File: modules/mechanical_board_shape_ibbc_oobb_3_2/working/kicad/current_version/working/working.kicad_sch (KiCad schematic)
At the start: 4 parts

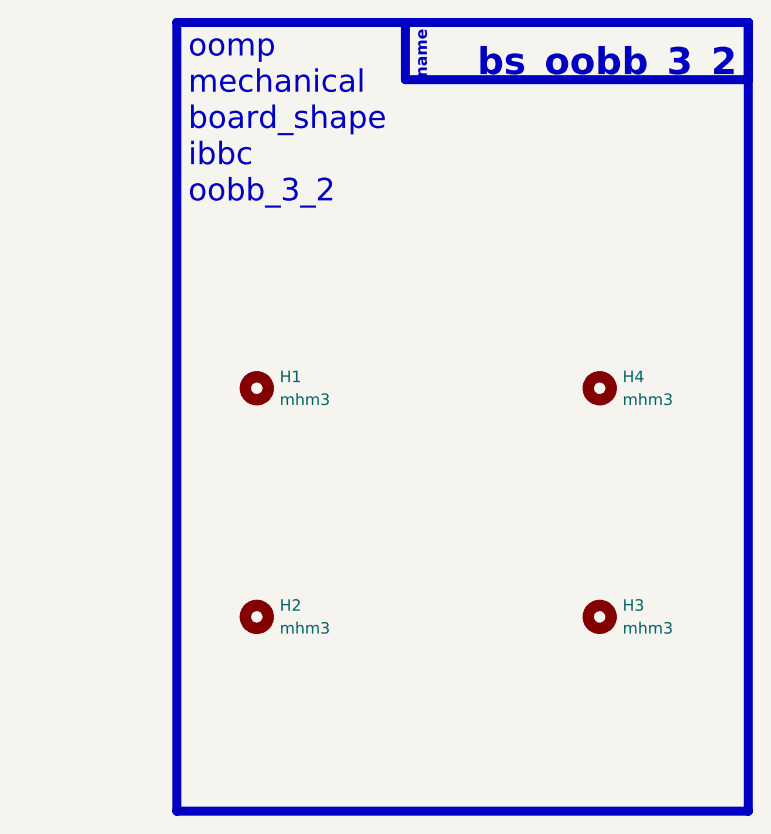
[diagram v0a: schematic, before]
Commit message: fixed formatting to be more consistent
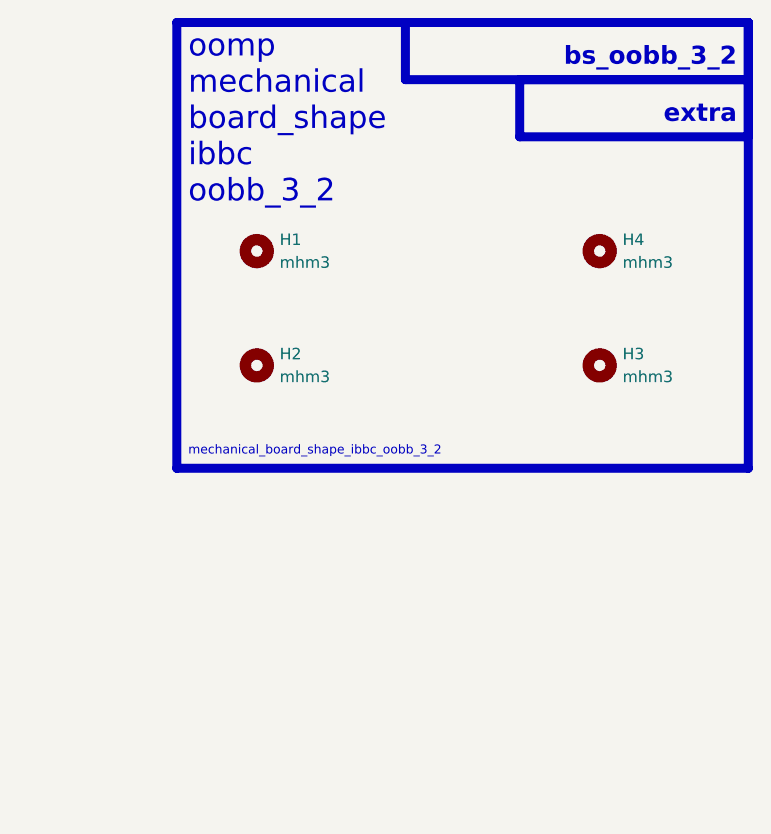
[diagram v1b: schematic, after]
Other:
- note added: "extra"
- note added: "mechanical_board_shape_ibbc_oobb_3_2"
- note removed: "name"
- moved on the sheet: H1, H2, H3, H4
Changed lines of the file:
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@@
 (kicad_sch (version 20230121) (generator eeschema)
   (paper "A4")
-  (rectangle (start 93.98 17.78) (end 157.48 105.41)
+  (rectangle (start 93.98 17.78) (end 157.48 67.31)
+    (stroke (width 1) (type default))
+    (fill (type none))
+  )
+  (rectangle (start 132.08 24.13) (end 157.48 30.48)
     (stroke (width 1) (type default))
     (fill (type none))
@@
   (rectangle (start 119.38 17.78) (end 157.48 24.13)
     (stroke (width 1) (type default))
-    (fill (type color) (color 0 0 0 0))
+    (fill (type none))
   )
   (rectangle (start 234.95 259.08) (end 234.95 259.08)
@@
     (fill (type none))
   )
-  (text "bs_oobb_3_2\n" (at 156.21 24.13 0)
-    (effects (font (size 3 3) (thickness 0.8) bold (color 255 255 255 1)) (justify right bottom))
+  (text "extra" (at 156.21 29.21 0)
+    (effects (font (size 2 2) (thickness 0.8) bold) (justify right bottom))
   )
-  (text "name" (at 121.92 24.13 90)
-    (effects (font (size 1.27 1.27) (thickness 0.254) bold (color 255 255 255 1)) (justify left bottom))
+  (text "bs_oobb_3_2\n" (at 156.21 22.86 0)
+    (effects (font (size 2 2) (thickness 0.8) bold) (justify right bottom))
+  )
+  (text "mechanical_board_shape_ibbc_oobb_3_2" (at 95.25 66.04 0)
+    (effects (font (size 1 1)) (justify left bottom))
   )
   (text "oomp\nmechanical\nboard_shape\nibbc\noobb_3_2" (at 95.25 38.1 0)
     (effects (font (size 2.5 2.5)) (justify left bottom))
   )
-  (symbol (lib_id "oomlout_oomp_part_symbols:mhm3_electronic_mounting_hole_m3") (at 102.87 83.82 0) (unit 1)
+  (symbol (lib_id "oomlout_oomp_part_symbols:mhm3_electronic_mounting_hole_m3") (at 102.87 55.88 0) (unit 1)
     (in_bom yes) (on_board yes) (dnp no) (fields_autoplaced)
-    (property "Reference" "H2" (at 105.41 82.55 0)
+    (property "Reference" "H2" (at 105.41 54.61 0)
       (effects (font (size 1.27 1.27)) (justify left))
     )
-    (property "Value" "mhm3" (at 105.41 85.09 0)
+    (property "Value" "mhm3" (at 105.41 57.15 0)
       (effects (font (size 1.27 1.27)) (justify left))
     )
-    (property "Footprint" "oomlout_oomp_part_footprints:mhm3_electronic_mounting_hole_m3" (at 102.87 83.82 0)
+    (property "Footprint" "oomlout_oomp_part_footprints:mhm3_electronic_mounting_hole_m3" (at 102.87 55.88 0)
       (effects (font (size 1.27 1.27)) hide)
     )
-    (property "Datasheet" "https://github.com/oomlout/oomlout_oomp_v3/parts/electronic_mounting_hole_m3/datasheet.pdf" (at 102.87 83.82 0)
+    (property "Datasheet" "https://github.com/oomlout/oomlout_oomp_v3/parts/electronic_mounting_hole_m3/datasheet.pdf" (at 102.87 55.88 0)
       (effects (font (size 1.27 1.27)) hide)
     )
@@
     )
   )
-  (symbol (lib_id "oomlout_oomp_part_symbols:mhm3_electronic_mounting_hole_m3") (at 140.97 58.42 0) (unit 1)
+  (symbol (lib_id "oomlout_oomp_part_symbols:mhm3_electronic_mounting_hole_m3") (at 140.97 43.18 0) (unit 1)
     (in_bom yes) (on_board yes) (dnp no) (fields_autoplaced)
-    (property "Reference" "H4" (at 143.51 57.15 0)
+    (property "Reference" "H4" (at 143.51 41.91 0)
       (effects (font (size 1.27 1.27)) (justify left))
     )
-    (property "Value" "mhm3" (at 143.51 59.69 0)
+    (property "Value" "mhm3" (at 143.51 44.45 0)
       (effects (font (size 1.27 1.27)) (justify left))
     )
-    (property "Footprint" "oomlout_oomp_part_footprints:mhm3_electronic_mounting_hole_m3" (at 140.97 58.42 0)
+    (property "Footprint" "oomlout_oomp_part_footprints:mhm3_electronic_mounting_hole_m3" (at 140.97 43.18 0)
       (effects (font (size 1.27 1.27)) hide)
     )
-    (property "Datasheet" "https://github.com/oomlout/oomlout_oomp_v3/parts/electronic_mounting_hole_m3/datasheet.pdf" (at 140.97 58.42 0)
+    (property "Datasheet" "https://github.com/oomlout/oomlout_oomp_v3/parts/electronic_mounting_hole_m3/datasheet.pdf" (at 140.97 43.18 0)
       (effects (font (size 1.27 1.27)) hide)
     )
@@
     )
   )
-  (symbol (lib_id "oomlout_oomp_part_symbols:mhm3_electronic_mounting_hole_m3") (at 102.87 58.42 0) (unit 1)
+  (symbol (lib_id "oomlout_oomp_part_symbols:mhm3_electronic_mounting_hole_m3") (at 102.87 43.18 0) (unit 1)
     (in_bom yes) (on_board yes) (dnp no) (fields_autoplaced)
-    (property "Reference" "H1" (at 105.41 57.15 0)
+    (property "Reference" "H1" (at 105.41 41.91 0)
       (effects (font (size 1.27 1.27)) (justify left))
     )
-    (property "Value" "mhm3" (at 105.41 59.69 0)
+    (property "Value" "mhm3" (at 105.41 44.45 0)
       (effects (font (size 1.27 1.27)) (justify left))
     )
-    (property "Footprint" "oomlout_oomp_part_footprints:mhm3_electronic_mounting_hole_m3" (at 102.87 58.42 0)
+    (property "Footprint" "oomlout_oomp_part_footprints:mhm3_electronic_mounting_hole_m3" (at 102.87 43.18 0)
       (effects (font (size 1.27 1.27)) hide)
     )
-    (property "Datasheet" "https://github.com/oomlout/oomlout_oomp_v3/parts/electronic_mounting_hole_m3/datasheet.pdf" (at 102.87 58.42 0)
+    (property "Datasheet" "https://github.com/oomlout/oomlout_oomp_v3/parts/electronic_mounting_hole_m3/datasheet.pdf" (at 102.87 43.18 0)
       (effects (font (size 1.27 1.27)) hide)
     )
@@
     )
   )
-  (symbol (lib_id "oomlout_oomp_part_symbols:mhm3_electronic_mounting_hole_m3") (at 140.97 83.82 0) (unit 1)
+  (symbol (lib_id "oomlout_oomp_part_symbols:mhm3_electronic_mounting_hole_m3") (at 140.97 55.88 0) (unit 1)
     (in_bom yes) (on_board yes) (dnp no) (fields_autoplaced)
-    (property "Reference" "H3" (at 143.51 82.55 0)
+    (property "Reference" "H3" (at 143.51 54.61 0)
       (effects (font (size 1.27 1.27)) (justify left))
     )
-    (property "Value" "mhm3" (at 143.51 85.09 0)
+    (property "Value" "mhm3" (at 143.51 57.15 0)
       (effects (font (size 1.27 1.27)) (justify left))
     )
-    (property "Footprint" "oomlout_oomp_part_footprints:mhm3_electronic_mounting_hole_m3" (at 140.97 83.82 0)
+    (property "Footprint" "oomlout_oomp_part_footprints:mhm3_electronic_mounting_hole_m3" (at 140.97 55.88 0)
       (effects (font (size 1.27 1.27)) hide)
     )
-    (property "Datasheet" "https://github.com/oomlout/oomlout_oomp_v3/parts/electronic_mounting_hole_m3/datasheet.pdf" (at 140.97 83.82 0)
+    (property "Datasheet" "https://github.com/oomlout/oomlout_oomp_v3/parts/electronic_mounting_hole_m3/datasheet.pdf" (at 140.97 55.88 0)
       (effects (font (size 1.27 1.27)) hide)
     )

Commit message: schematic formatting
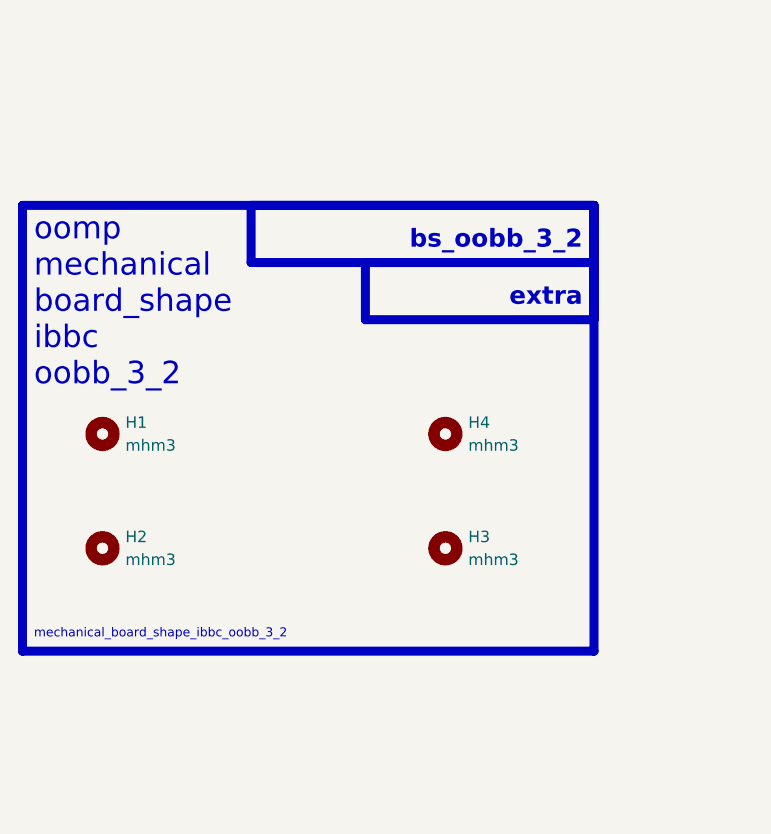
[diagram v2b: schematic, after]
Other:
- moved on the sheet: H1, H2, H3, H4
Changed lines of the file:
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@@
 (kicad_sch (version 20230121) (generator eeschema)
-  (paper "A4")
-  (rectangle (start 93.98 17.78) (end 157.48 67.31)
+  (paper "A5")
+  (rectangle (start 76.835 38.1) (end 140.335 87.63)
     (stroke (width 1) (type default))
     (fill (type none))
   )
-  (rectangle (start 132.08 24.13) (end 157.48 30.48)
+  (rectangle (start 114.935 44.45) (end 140.335 50.8)
     (stroke (width 1) (type default))
     (fill (type none))
   )
-  (rectangle (start 119.38 17.78) (end 157.48 24.13)
+  (rectangle (start 102.235 38.1) (end 140.335 44.45)
     (stroke (width 1) (type default))
     (fill (type none))
   )
-  (rectangle (start 234.95 259.08) (end 234.95 259.08)
+  (rectangle (start 217.805 279.4) (end 217.805 279.4)
     (stroke (width 0) (type default))
     (fill (type none))
   )
-  (rectangle (start 233.68 215.9) (end 233.68 215.9)
+  (rectangle (start 216.535 236.22) (end 216.535 236.22)
     (stroke (width 0) (type default))
     (fill (type none))
   )
-  (text "extra" (at 156.21 29.21 0)
+  (text "extra" (at 139.065 49.53 0)
     (effects (font (size 2 2) (thickness 0.8) bold) (justify right bottom))
   )
-  (text "bs_oobb_3_2\n" (at 156.21 22.86 0)
+  (text "bs_oobb_3_2\n" (at 139.065 43.18 0)
     (effects (font (size 2 2) (thickness 0.8) bold) (justify right bottom))
   )
-  (text "mechanical_board_shape_ibbc_oobb_3_2" (at 95.25 66.04 0)
+  (text "mechanical_board_shape_ibbc_oobb_3_2" (at 78.105 86.36 0)
     (effects (font (size 1 1)) (justify left bottom))
   )
-  (text "oomp\nmechanical\nboard_shape\nibbc\noobb_3_2" (at 95.25 38.1 0)
+  (text "oomp\nmechanical\nboard_shape\nibbc\noobb_3_2" (at 78.105 58.42 0)
     (effects (font (size 2.5 2.5)) (justify left bottom))
   )
-  (symbol (lib_id "oomlout_oomp_part_symbols:mhm3_electronic_mounting_hole_m3") (at 102.87 55.88 0) (unit 1)
+  (symbol (lib_id "oomlout_oomp_part_symbols:mhm3_electronic_mounting_hole_m3") (at 85.725 76.2 0) (unit 1)
     (in_bom yes) (on_board yes) (dnp no) (fields_autoplaced)
-    (property "Reference" "H2" (at 105.41 54.61 0)
+    (property "Reference" "H2" (at 88.265 74.93 0)
       (effects (font (size 1.27 1.27)) (justify left))
     )
-    (property "Value" "mhm3" (at 105.41 57.15 0)
+    (property "Value" "mhm3" (at 88.265 77.47 0)
       (effects (font (size 1.27 1.27)) (justify left))
     )
-    (property "Footprint" "oomlout_oomp_part_footprints:mhm3_electronic_mounting_hole_m3" (at 102.87 55.88 0)
+    (property "Footprint" "oomlout_oomp_part_footprints:mhm3_electronic_mounting_hole_m3" (at 85.725 76.2 0)
       (effects (font (size 1.27 1.27)) hide)
     )
-    (property "Datasheet" "https://github.com/oomlout/oomlout_oomp_v3/parts/electronic_mounting_hole_m3/datasheet.pdf" (at 102.87 55.88 0)
+    (property "Datasheet" "https://github.com/oomlout/oomlout_oomp_v3/parts/electronic_mounting_hole_m3/datasheet.pdf" (at 85.725 76.2 0)
       (effects (font (size 1.27 1.27)) hide)
     )
@@
     )
   )
-  (symbol (lib_id "oomlout_oomp_part_symbols:mhm3_electronic_mounting_hole_m3") (at 140.97 43.18 0) (unit 1)
+  (symbol (lib_id "oomlout_oomp_part_symbols:mhm3_electronic_mounting_hole_m3") (at 123.825 63.5 0) (unit 1)
     (in_bom yes) (on_board yes) (dnp no) (fields_autoplaced)
-    (property "Reference" "H4" (at 143.51 41.91 0)
+    (property "Reference" "H4" (at 126.365 62.23 0)
       (effects (font (size 1.27 1.27)) (justify left))
     )
-    (property "Value" "mhm3" (at 143.51 44.45 0)
+    (property "Value" "mhm3" (at 126.365 64.77 0)
       (effects (font (size 1.27 1.27)) (justify left))
     )
-    (property "Footprint" "oomlout_oomp_part_footprints:mhm3_electronic_mounting_hole_m3" (at 140.97 43.18 0)
+    (property "Footprint" "oomlout_oomp_part_footprints:mhm3_electronic_mounting_hole_m3" (at 123.825 63.5 0)
       (effects (font (size 1.27 1.27)) hide)
     )
-    (property "Datasheet" "https://github.com/oomlout/oomlout_oomp_v3/parts/electronic_mounting_hole_m3/datasheet.pdf" (at 140.97 43.18 0)
+    (property "Datasheet" "https://github.com/oomlout/oomlout_oomp_v3/parts/electronic_mounting_hole_m3/datasheet.pdf" (at 123.825 63.5 0)
       (effects (font (size 1.27 1.27)) hide)
     )
@@
     )
   )
-  (symbol (lib_id "oomlout_oomp_part_symbols:mhm3_electronic_mounting_hole_m3") (at 102.87 43.18 0) (unit 1)
+  (symbol (lib_id "oomlout_oomp_part_symbols:mhm3_electronic_mounting_hole_m3") (at 85.725 63.5 0) (unit 1)
     (in_bom yes) (on_board yes) (dnp no) (fields_autoplaced)
-    (property "Reference" "H1" (at 105.41 41.91 0)
+    (property "Reference" "H1" (at 88.265 62.23 0)
       (effects (font (size 1.27 1.27)) (justify left))
     )
-    (property "Value" "mhm3" (at 105.41 44.45 0)
+    (property "Value" "mhm3" (at 88.265 64.77 0)
       (effects (font (size 1.27 1.27)) (justify left))
     )
-    (property "Footprint" "oomlout_oomp_part_footprints:mhm3_electronic_mounting_hole_m3" (at 102.87 43.18 0)
+    (property "Footprint" "oomlout_oomp_part_footprints:mhm3_electronic_mounting_hole_m3" (at 85.725 63.5 0)
       (effects (font (size 1.27 1.27)) hide)
     )
-    (property "Datasheet" "https://github.com/oomlout/oomlout_oomp_v3/parts/electronic_mounting_hole_m3/datasheet.pdf" (at 102.87 43.18 0)
+    (property "Datasheet" "https://github.com/oomlout/oomlout_oomp_v3/parts/electronic_mounting_hole_m3/datasheet.pdf" (at 85.725 63.5 0)
       (effects (font (size 1.27 1.27)) hide)
     )
@@
     )
   )
-  (symbol (lib_id "oomlout_oomp_part_symbols:mhm3_electronic_mounting_hole_m3") (at 140.97 55.88 0) (unit 1)
+  (symbol (lib_id "oomlout_oomp_part_symbols:mhm3_electronic_mounting_hole_m3") (at 123.825 76.2 0) (unit 1)
     (in_bom yes) (on_board yes) (dnp no) (fields_autoplaced)
-    (property "Reference" "H3" (at 143.51 54.61 0)
+    (property "Reference" "H3" (at 126.365 74.93 0)
       (effects (font (size 1.27 1.27)) (justify left))
     )
-    (property "Value" "mhm3" (at 143.51 57.15 0)
+    (property "Value" "mhm3" (at 126.365 77.47 0)
       (effects (font (size 1.27 1.27)) (justify left))
     )
-    (property "Footprint" "oomlout_oomp_part_footprints:mhm3_electronic_mounting_hole_m3" (at 140.97 55.88 0)
+    (property "Footprint" "oomlout_oomp_part_footprints:mhm3_electronic_mounting_hole_m3" (at 123.825 76.2 0)
       (effects (font (size 1.27 1.27)) hide)
     )
-    (property "Datasheet" "https://github.com/oomlout/oomlout_oomp_v3/parts/electronic_mounting_hole_m3/datasheet.pdf" (at 140.97 55.88 0)
+    (property "Datasheet" "https://github.com/oomlout/oomlout_oomp_v3/parts/electronic_mounting_hole_m3/datasheet.pdf" (at 123.825 76.2 0)
       (effects (font (size 1.27 1.27)) hide)
     )
